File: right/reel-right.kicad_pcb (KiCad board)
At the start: 2 copper layers, 134.6 x 86.9 mm, 46 parts, among them J1 Conn_01x02, SW1 SW_Push, SW10 SW_Push, SW11 SW_Push, SW12 SW_Push, SW13 SW_Push, SW14 SW_Push, SW15 SW_Push, SW16 SW_Push, SW17 SW_Push, SW18 SW_Push, SW19 SW_Push, SW2 SW_Push, SW22 SW_SPDT, SW3 SW_Push, SW4 SW_Push, SW5 SW_Push, SW6 SW_Push, SW7 SW_Push, SW8 SW_Push, SW9 SW_Push

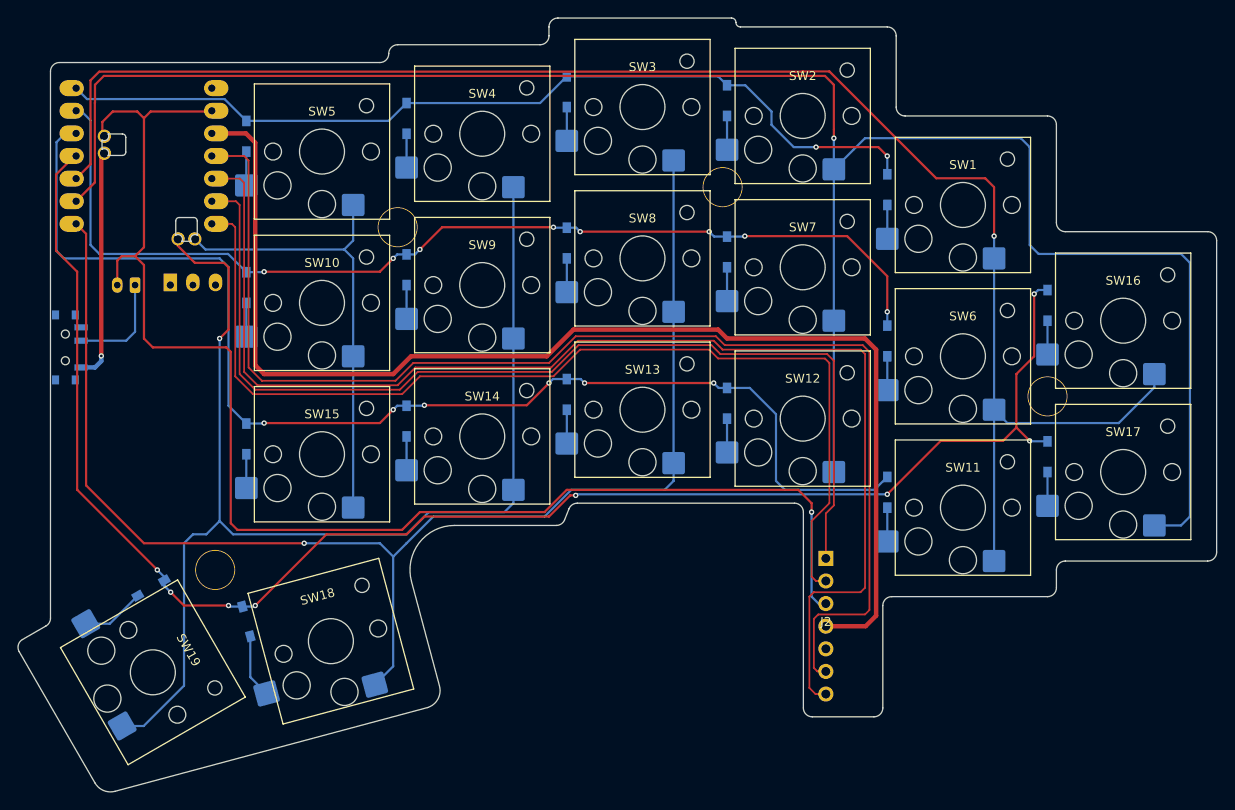
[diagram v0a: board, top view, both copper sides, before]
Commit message: Update ReeL switch footprints and board layouts
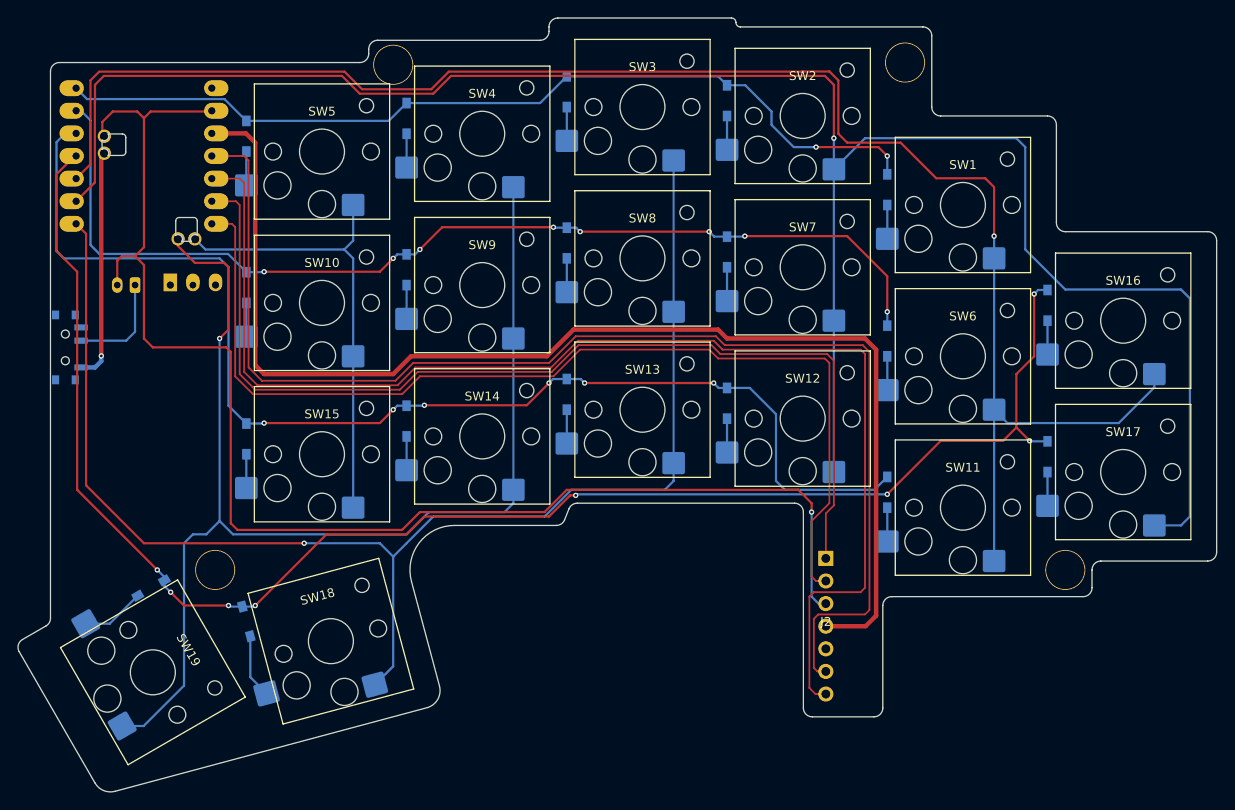
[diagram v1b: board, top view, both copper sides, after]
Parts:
- moved Ref** 24.8 mm to (145.5, 50.5)
- moved Ref** 19.6 mm to (163.5, 107.5)
- moved Ref** 18.3 mm to (88.0, 50.8)
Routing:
- net Col0: track 182.8 -> 187.9 mm
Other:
- outline, holes or cut-outs redrawn

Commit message: Update right board fabrication outputs
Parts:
- moved J2 3.47 mm to (139.0, 116.3)
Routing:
- net GND: track 155.4 -> 160.2 mm
- net SCLK: track 115.1 -> 117.5 mm
- net nCS: track 116.4 -> 118.5 mm
- net MOTION: track 143.4 -> 144.5 mm
- net SDIO: track 143.4 -> 144.3 mm
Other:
- outline, holes or cut-outs redrawn
